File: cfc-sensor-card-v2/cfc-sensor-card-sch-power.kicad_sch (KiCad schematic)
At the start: 65 parts, among them U10 LT3042IMSE, U11 LT3042IMSE, U5 TLC3704IPWR, U6 LP2985-3.3, U7 LT3042IMSE, U8 LT3042IMSE, U9 LT3042IMSE

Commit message: Update
updated opd address resistors to 100 ohms from 100 ohms, changed the 100 ohm res VBUSP to 10 ohms. Updated TEC page for sensor to have bidirectional current sense for diag. Removed misc testpoints
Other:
- note added: ""PIRT""
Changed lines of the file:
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@@
+		)
+	)
+	(text "\"PIRT\""
+		(exclude_from_sim no)
+		(at 149.86 148.336 0)
+		(effects
+			(font
+				(size 1.27 1.27)
+			)
+			(justify left bottom)
 		)
 	)

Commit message: Processor board routing
Completed rework and routing of processor board. No drc errors or warnings. Ready for design review on processor board. Minor changes to schematic for easier routing on pull down resistors connected to the octavo SIP. Reannotated sensor schematic component designators.
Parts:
- renumbered C9 to C11, C11 to C12, C12 to C13, C10 to C14, C13 to C15, C14 to C16, C15 to C17, C16 to C18, C17 to C19, C18 to C20, C19 to C21, C20 to C22, C21 to C23, C22 to C24, C23 to C25, C24 to C26, C25 to C27, C26 to C28, C27 to C29, C28 to C30, R37 to R39, R38 to R40, R39 to R41, R40 to R42, R41 to R43, R42 to R44, R43 to R45, R44 to R46, R45 to R47, R46 to R48, R47 to R49, R48 to R50, R49 to R51, R50 to R52, R51 to R53, R52 to R54, R53 to R55, R54 to R56, R55 to R57, R56 to R58, TP21 to TP11, TP5 to TP12, TP22 to TP13, TP24 to TP14, TP25 to TP15, TP26 to TP16, TP27 to TP17, TP29 to TP18, TP31 to TP19, TP33 to TP20, TP35 to TP21, TP37 to TP22, TP8 to TP23, TP9 to TP24, TP10 to TP25, TP12 to TP26, TP11 to TP27, U6 to U5, U5 to U6

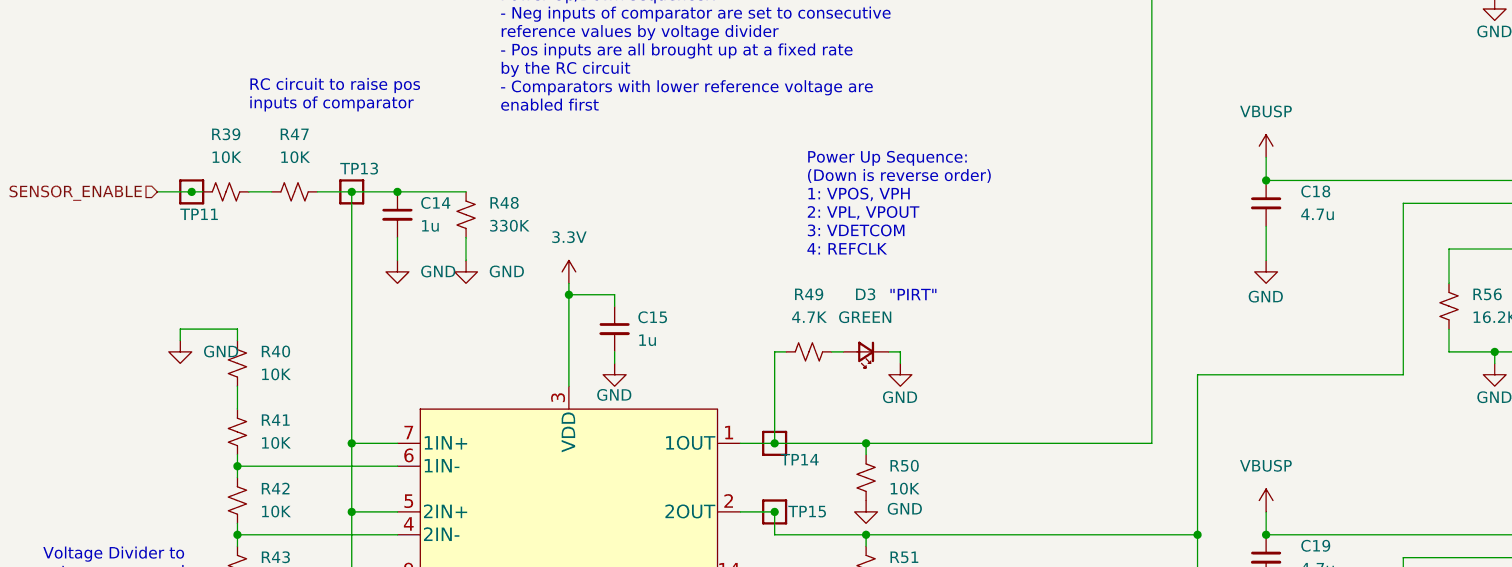
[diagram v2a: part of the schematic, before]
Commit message: Update
Updated BOM, couple of fixes on OPD. Minor routing and layout changes. Removed logic gates from sensor card.
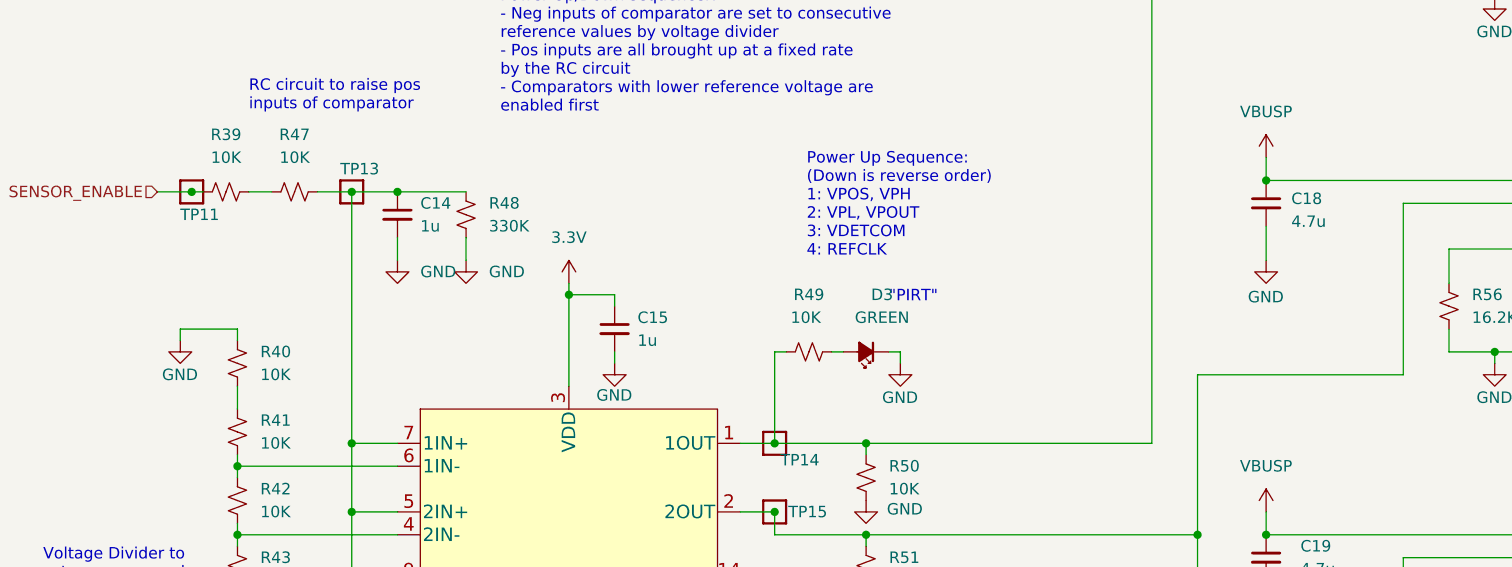
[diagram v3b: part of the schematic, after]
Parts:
- C21, C22, C23, C24, C25: DPN 587-3476-1-ND -> 399-C0603C474K3RACAUTOCT-ND; MFR Taiyo Yuden -> KEMET; MPN TMK107BJ474KAHT -> C0603C474K3RACAUTO
- D3: symbol Device:LED_Small -> Device:LED_Small_Filled
- R49: value 4.7K -> 10K; DPN RMCF0603FT4K70CT-ND -> RMCF0603FT10K0CT-ND; MPN RMCF0603FT4K70 -> RMCF0603FT10K0
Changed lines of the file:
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@@
 			)
 		)
-		(property "Datasheet" "https://mm.digikey.com/Volume0/opasdata/d220001/medias/docus/1875/TMK107BJ474KAHT_SS.pdf"
+		(property "Datasheet" "https://www.yageogroup.com/content/datasheet/asset/file/KEM_C1023_X7R_AUTO_SMD"
 			(at 222.25 67.31 0)
 			(hide yes)
@@
 			)
 		)
-		(property "Description" "0.47 µF ±10% 25V Ceramic Capacitor X5R 0603 (1608 Metric)"
+		(property "Description" "0.47 µF ±10% 25V Ceramic Capacitor X7R 0603 (1608 Metric)"
 			(at 222.25 67.31 0)
 			(hide yes)
@@
 			)
 		)
-		(property "DPN" "587-3476-1-ND"
+		(property "DPN" "399-C0603C474K3RACAUTOCT-ND"
 			(at 222.25 67.31 0)
 			(hide yes)
@@
 			)
 		)
-		(property "MFR" "Taiyo Yuden"
+		(property "MFR" "KEMET"
 			(at 222.25 67.31 0)
 			(hide yes)
@@
 			)
 		)
-		(property "MPN" "TMK107BJ474KAHT"
+		(property "MPN" "C0603C474K3RACAUTO"
 			(at 222.25 67.31 0)
 			(hide yes)
@@
 			)
 		)
-		(property "Datasheet" "https://mm.digikey.com/Volume0/opasdata/d220001/medias/docus/1875/TMK107BJ474KAHT_SS.pdf"
+		(property "Datasheet" "https://www.yageogroup.com/content/datasheet/asset/file/KEM_C1023_X7R_AUTO_SMD"
 			(at 222.25 187.96 0)
 			(hide yes)
@@
 			)
 		)
-		(property "Description" "0.47 µF ±10% 25V Ceramic Capacitor X5R 0603 (1608 Metric)"
+		(property "Description" "0.47 µF ±10% 25V Ceramic Capacitor X7R 0603 (1608 Metric)"
 			(at 222.25 187.96 0)
 			(hide yes)
@@
 			)
 		)
-		(property "DPN" "587-3476-1-ND"
+		(property "DPN" "399-C0603C474K3RACAUTOCT-ND"
 			(at 222.25 187.96 0)
 			(hide yes)
@@
 			)
 		)
-		(property "MFR" "Taiyo Yuden"
+		(property "MFR" "KEMET"
 			(at 222.25 187.96 0)
 			(hide yes)
@@
 			)
 		)
-		(property "MPN" "TMK107BJ474KAHT"
+		(property "MPN" "C0603C474K3RACAUTO"
 			(at 222.25 187.96 0)
 			(hide yes)
@@
 		(in_pos_files yes)
 		(dnp no)
-		(fields_autoplaced yes)
 		(property "Reference" "R49"
 			(at 140.97 147.32 90)
@@
 			)
 		)
-		(property "Value" "4.7K"
-			(at 140.97 149.86 90)
+		(property "Value" "10K"
+			(at 138.938 149.86 90)
 			(show_name no)
 			(do_not_autoplace no)
@@
 					(size 1.27 1.27)
 				)
+				(justify right)
 			)
 		)
@@
 			)
 		)
-		(property "Description" "4.7 kOhms ±1% 0.1W, 1/10W Chip Resistor 0603 (1608 Metric) Automotive AEC-Q200 Thick Film"
+		(property "Description" "10 kOhms ±1% 0.1W, 1/10W Chip Resistor 0603 (1608 Metric) Automotive AEC-Q200 Thick Film"
 			(at 140.97 153.67 0)
 			(hide yes)
@@
 			)
 		)
-		(property "DPN" "RMCF0603FT4K70CT-ND"
+		(property "DPN" "RMCF0603FT10K0CT-ND"
 			(at 140.97 153.67 90)
 			(hide yes)
@@
 			)
 		)
-		(property "MPN" "RMCF0603FT4K70"
+		(property "MPN" "RMCF0603FT10K0"
 			(at 140.97 153.67 90)
 			(hide yes)
@@
 		(in_pos_files yes)
 		(dnp no)
-		(fields_autoplaced yes)
 		(property "Reference" "#GND027"
 			(at 71.12 158.75 0)
@@
 		)
 		(property "Value" "GND"
-			(at 73.66 153.6699 0)
+			(at 69.088 156.21 0)
 			(show_name no)
 			(do_not_autoplace no)
@@
 			)
 		)
-		(property "Datasheet" "https://mm.digikey.com/Volume0/opasdata/d220001/medias/docus/1875/TMK107BJ474KAHT_SS.pdf"
+		(property "Datasheet" "https://www.yageogroup.com/content/datasheet/asset/file/KEM_C1023_X7R_AUTO_SMD"
 			(at 222.25 228.6 0)
 			(hide yes)
@@
 			)
 		)
-		(property "Description" "0.47 µF ±10% 25V Ceramic Capacitor X5R 0603 (1608 Metric)"
+		(property "Description" "0.47 µF ±10% 25V Ceramic Capacitor X7R 0603 (1608 Metric)"
 			(at 222.25 228.6 0)
 			(hide yes)
@@
 			)
 		)
-		(property "DPN" "587-3476-1-ND"
+		(property "DPN" "399-C0603C474K3RACAUTOCT-ND"
 			(at 222.25 228.6 0)
 			(hide yes)
@@
 			)
 		)
-		(property "MFR" "Taiyo Yuden"
+		(property "MFR" "KEMET"
 			(at 222.25 228.6 0)
 			(hide yes)
@@
 			)
 		)
-		(property "MPN" "TMK107BJ474KAHT"
+		(property "MPN" "C0603C474K3RACAUTO"
 			(at 222.25 228.6 0)
 			(hide yes)
@@
 	)
 	(symbol
-		(lib_id "Device:LED_Small")
+		(lib_id "Device:LED_Small_Filled")
 		(at 147.32 153.67 180)
 		(unit 1)
@@
 		(in_pos_files yes)
 		(dnp no)
-		(fields_autoplaced yes)
 		(property "Reference" "D3"
-			(at 147.2565 147.32 0)
+			(at 149.098 147.32 0)
 			(show_name no)
 			(do_not_autoplace no)
@@
 		)
 		(property "Value" "GREEN"
-			(at 147.2565 149.86 0)
+			(at 149.098 149.86 0)
 			(show_name no)
 			(do_not_autoplace no)
@@
 			)
 		)
-		(property "Description" "Light emitting diode, small symbol"
+		(property "Description" "Light emitting diode, small symbol, filled shape"
 			(at 147.32 153.67 0)
 			(hide yes)
@@
 			)
 		)
-		(property "Datasheet" "https://mm.digikey.com/Volume0/opasdata/d220001/medias/docus/1875/TMK107BJ474KAHT_SS.pdf"
+		(property "Datasheet" "https://www.yageogroup.com/content/datasheet/asset/file/KEM_C1023_X7R_AUTO_SMD"
 			(at 222.25 148.59 0)
 			(hide yes)
@@
 			)
 		)
-		(property "Description" "0.47 µF ±10% 25V Ceramic Capacitor X5R 0603 (1608 Metric)"
+		(property "Description" "0.47 µF ±10% 25V Ceramic Capacitor X7R 0603 (1608 Metric)"
 			(at 222.25 148.59 0)
 			(hide yes)
@@
 			)
 		)
-		(property "DPN" "587-3476-1-ND"
+		(property "DPN" "399-C0603C474K3RACAUTOCT-ND"
 			(at 222.25 148.59 0)
 			(hide yes)
@@
 			)
 		)
-		(property "MFR" "Taiyo Yuden"
+		(property "MFR" "KEMET"
 			(at 222.25 148.59 0)
 			(hide yes)
@@
 			)
 		)
-		(property "MPN" "TMK107BJ474KAHT"
+		(property "MPN" "C0603C474K3RACAUTO"
 			(at 222.25 148.59 0)
 			(hide yes)
@@
 		(in_pos_files yes)
 		(dnp no)
-		(fields_autoplaced yes)
 		(property "Reference" "C18"
-			(at 195.58 135.8899 0)
+			(at 194.564 136.652 0)
 			(show_name no)
 			(do_not_autoplace no)
@@
 		)
 		(property "Value" "4.7u"
-			(at 195.58 138.4299 0)
+			(at 194.564 139.192 0)
 			(show_name no)
 			(do_not_autoplace no)
@@
 			)
 		)
-		(property "Datasheet" "https://mm.digikey.com/Volume0/opasdata/d220001/medias/docus/1875/TMK107BJ474KAHT_SS.pdf"
+		(property "Datasheet" "https://www.yageogroup.com/content/datasheet/asset/file/KEM_C1023_X7R_AUTO_SMD"
 			(at 222.25 107.95 0)
 			(hide yes)
@@
 			)
 		)
-		(property "Description" "0.47 µF ±10% 25V Ceramic Capacitor X5R 0603 (1608 Metric)"
+		(property "Description" "0.47 µF ±10% 25V Ceramic Capacitor X7R 0603 (1608 Metric)"
 			(at 222.25 107.95 0)
 			(hide yes)
@@
 			)
 		)
-		(property "DPN" "587-3476-1-ND"
+		(property "DPN" "399-C0603C474K3RACAUTOCT-ND"
 			(at 222.25 107.95 0)
 			(hide yes)
@@
 			)
 		)
-		(property "MFR" "Taiyo Yuden"
+		(property "MFR" "KEMET"
 			(at 222.25 107.95 0)
 			(hide yes)
@@
 			)
 		)
-		(property "MPN" "TMK107BJ474KAHT"
+		(property "MPN" "C0603C474K3RACAUTO"
 			(at 222.25 107.95 0)
 			(hide yes)
